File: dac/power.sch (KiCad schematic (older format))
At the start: 47 parts, among them J5 Aux power, Q1 2STD1665T4, U3 OPA1611, U4 MCP1755S-3302E/DB, U5 NCP1117STAT3G, U6 LM337_SOT223

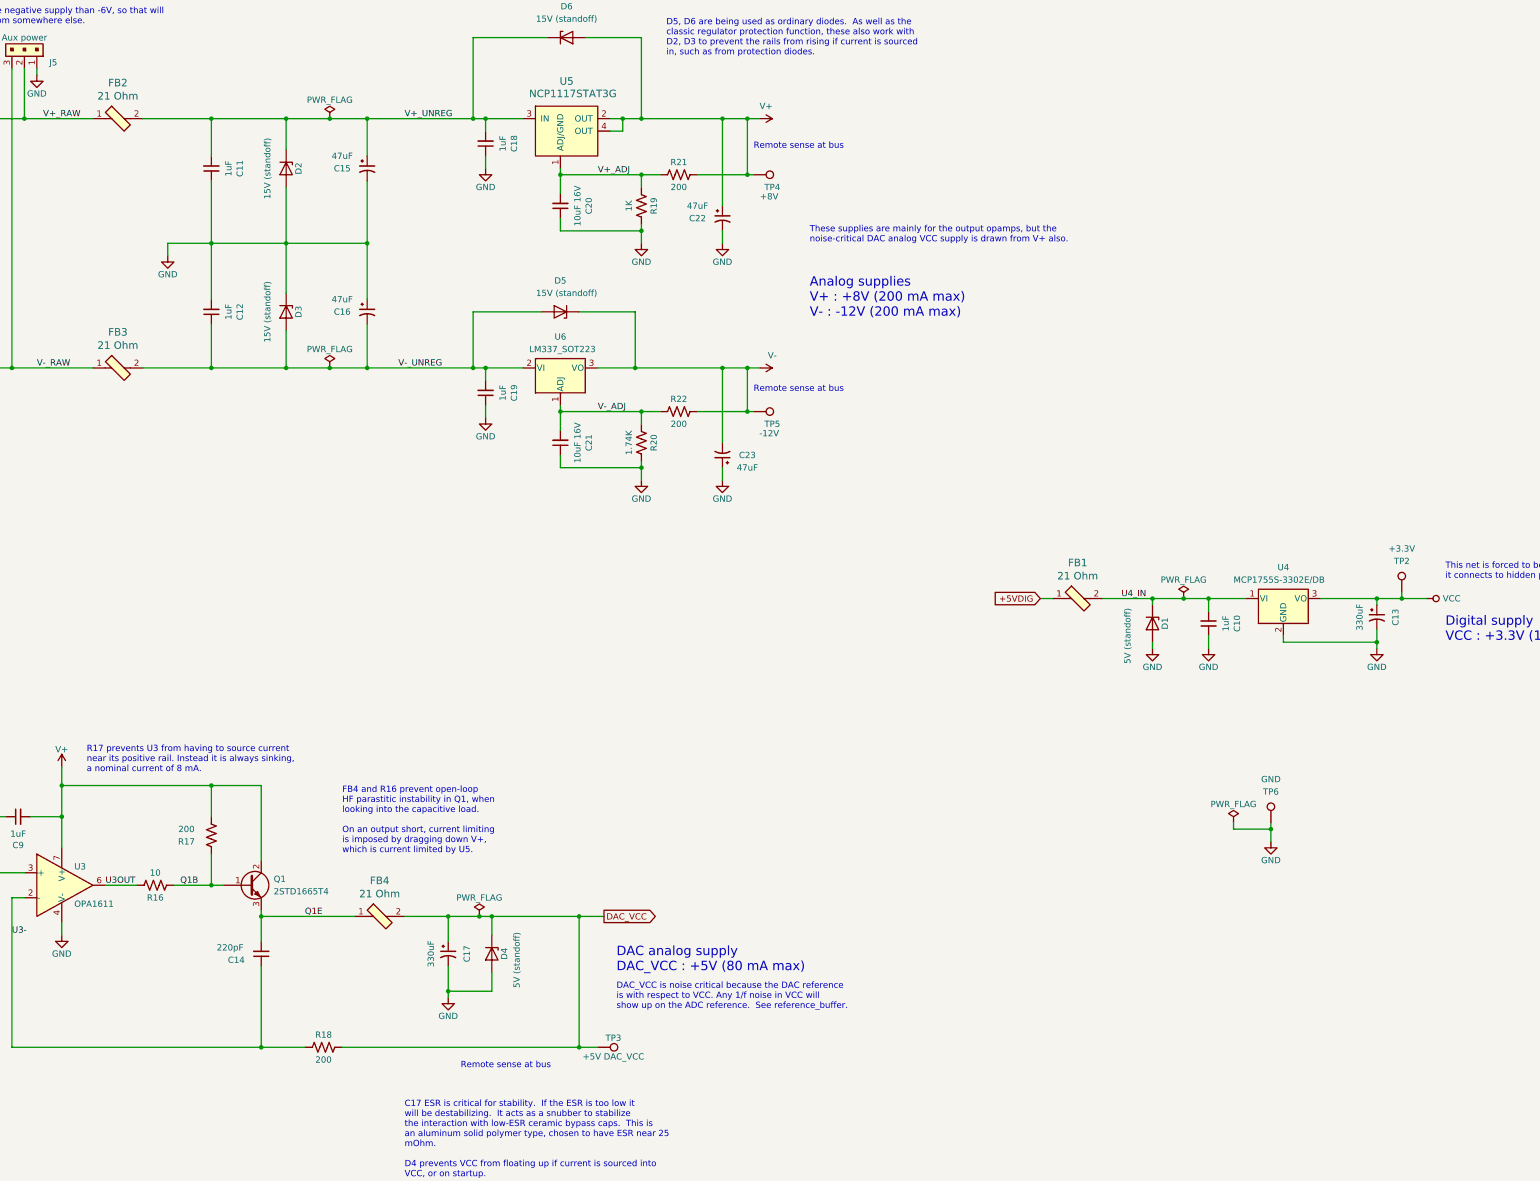
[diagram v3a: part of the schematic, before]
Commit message: Everything seems ready to go for the DAC board.  Made my BOM and checked it twice. Checked footprints of new components and fixed J5, R7-R10.
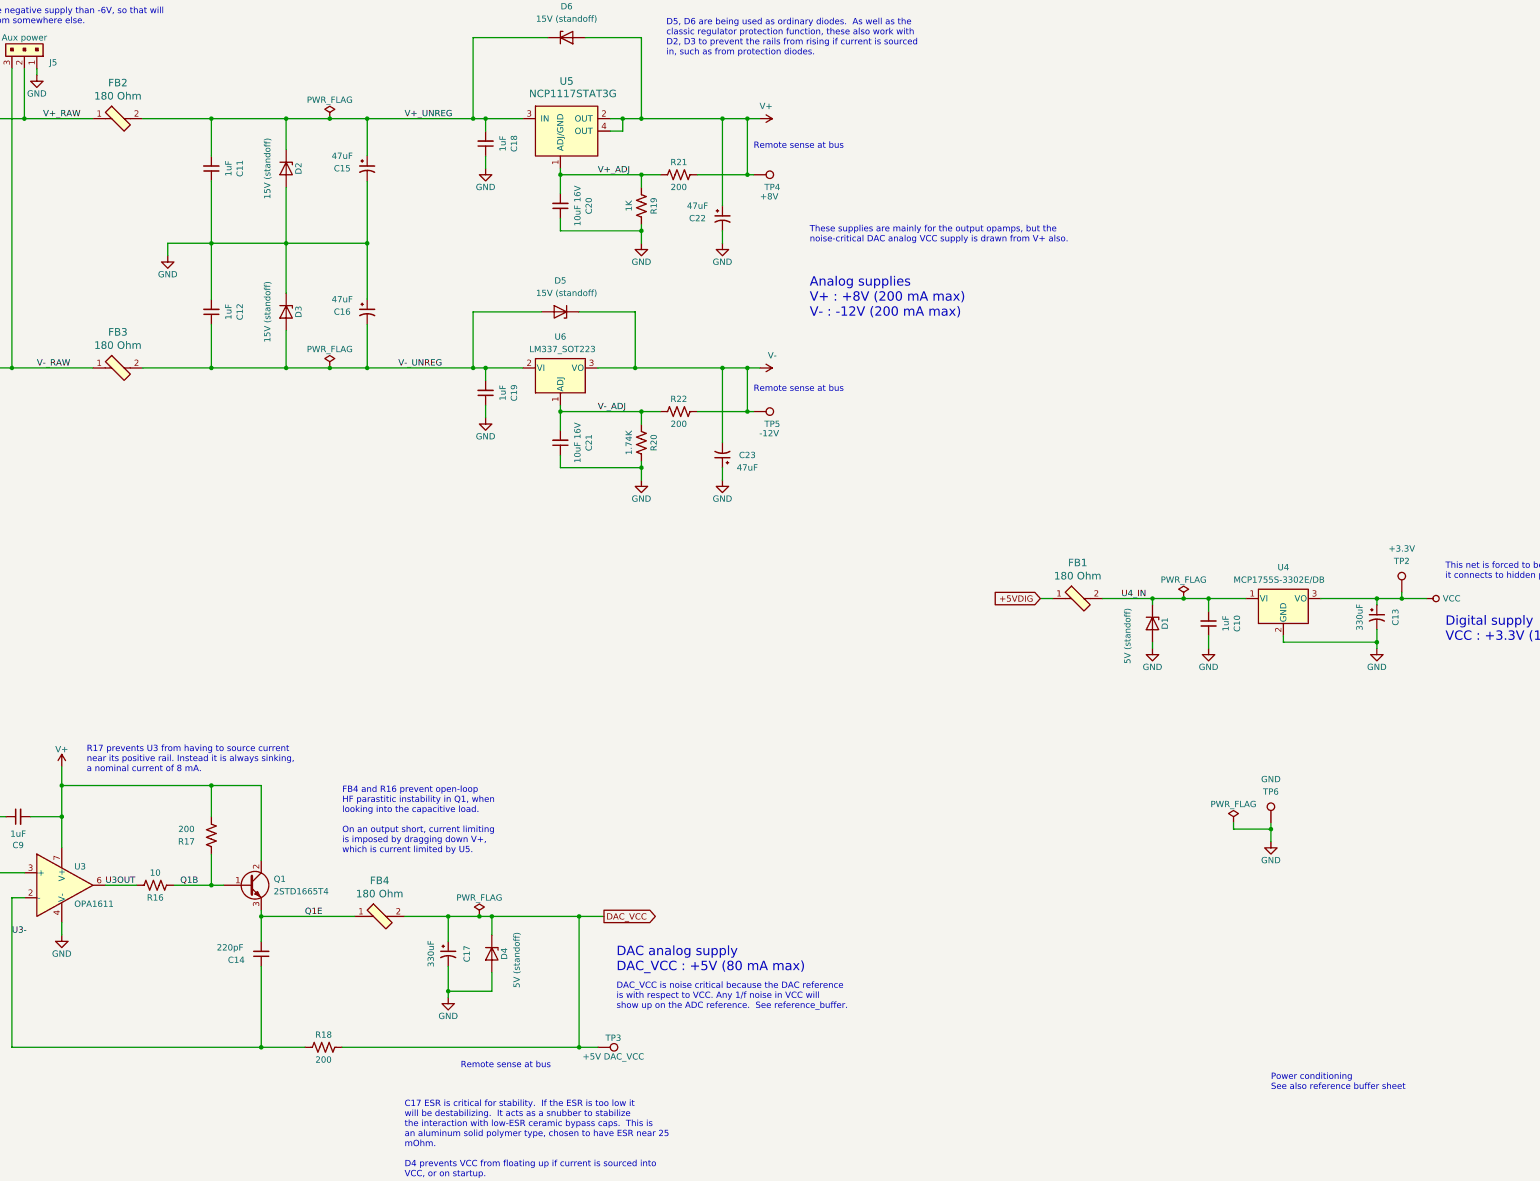
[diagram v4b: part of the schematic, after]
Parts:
- C10, C11, C12, C18, C19, C9: DK line 27 -> I.27
- C13, C17: DK line 19 -> I.19
- C14: DK line 44 -> M.15; Description (none) -> CAP CER 220PF 50V C0G/NP0 0603; Digikey (none) -> 1276-1048-1-ND; MPN (none) -> CL10C221JB8NNNC; Manufacturer (none) -> Samsung Electro-Mechanics
- C15, C16, C22, C23: DK line (none) -> D.5
- C20, C21, C8: DK line 10 -> M.10
- D1, D4: DK line 40 -> I.40
- D2, D3, D5, D6: DK line (none) -> D.39; Description (none) -> TVS DIODE 15V 24.4V SMA; Digikey (none) -> SMAJ15A-FDICT-ND; MPN (none) -> SMAJ15A-13-F; Manufacturer (none) -> Diodes Incorporated
- FB1, FB2, FB3, FB4: value 21 Ohm -> 180 Ohm; DK line 24 -> M.36; Description FERRITE BEAD 21 OHM 0805, 100 nH, 5 mOhm -> FERRITE BEAD 180 OHM 0805 1LN; Digikey 587-1765-1-ND -> 732-6123-1-ND; MPN FBMJ2125HM210NT -> 74279220181; Manufacturer Taiyo Yuden -> Würth Elektronik
- J5: footprint digikey-footprints:PinHeader_1x3_P2.54_Drill1.1mm -> input:molex_kk100_PinHeader_1x3_P2.54_Drill1.1mm; DK line (none) -> D.31; DK_Datasheet_Link https://www.te.com/commerce/DocumentDelivery/DDEController?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 -> (none); DK_Detail_Page /product-detail/en/te-connectivity-amp-connectors/640456-3/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 -> (none); Digi-Key_PN A19470-ND -> (none); Digikey (none) -> WM4201-ND; Family Rectangular Connectors - Headers, Male Pins -> (none); MPN 640456-3 -> 0022232031; Manufacturer TE Connectivity AMP Connectors -> Molex; Status Active -> (none)
- Q1: DK line 22 -> I.22
- R13, R19: DK line (none) -> M.31; Description (none) -> RES 1K OHM 1% 1/8W 0603; Digikey (none) -> RNCP0603FTD1K00CT-ND; MPN (none) -> RNCP0603FTD1K00; Manufacturer (none) -> Stackpole Electronics Inc
- R14, R15: DK line (none) -> M.12; Description (none) -> RES 0 OHM JUMPER 1/10W 0603; Digikey (none) -> RMCF0603ZT0R00CT-ND; MPN (none) -> RMCF0603ZT0R00; Manufacturer (none) -> Stackpole Electronics Inc
- R16: DK line 52 -> I.52
- R17, R18, R21, R22: DK line 55 -> I.55
- R20: DK line (none) -> D.33; Description (none) -> RES 1.74K OHM 1% 1/10W 0603; Digikey (none) -> RMCF0603FT1K74CT-ND; MPN (none) -> RMCF0603FT1K74; Manufacturer (none) -> Stackpole Electronics Inc
- TP2, TP3, TP4, TP5: Description Do Not Populate -> Optional Keystone 5000-5004; Manufacturer (none) -> Keystone Electronics
- TP6: DK line 33 -> I.33
- U3: DK line (none) -> D.2; Description (none) -> IC AUDIO 1 CIRCUIT 8SOIC; Digikey (none) -> 296-47811-1-ND; MPN (none) -> OPA1611AIDR; Manufacturer (none) -> Texas Instruments
- U4: DK line 25 -> I.25
- U5: DK line 26 -> I.26
- U6: DK line (none) -> D.6; Description (none) -> IC REG LIN NEG ADJ 1A SOT223-4; Digikey (none) -> LM337IMPX/NOPBCT-ND; MPN (none) -> LM337IMPX/NOPB; Manufacturer (none) -> Texas Instruments
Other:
- note added: "Power conditioning\nSee also reference buffer sheet"

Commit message: Mainly BOM tweaks, working on setting up more systematic database of parts and BOMs in parts/
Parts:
- R16: DK line I.52 -> I.9; Description RES SMD 10 OHM 5% 1/2W 0805 -> RES SMD 10 OHM 5% 0.4W 0805; MPN CRCW080510R0JNEAHP -> ESR10EZPJ100; Manufacturer Vishay Dale -> Rohm Semiconductor
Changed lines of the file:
@@
 F 1 "10" V 3400 7950 50  0000 C CNN
 F 2 "Resistor_SMD:R_0805_2012Metric" V 3540 7940 50  0001 C CNN
-F 3 "http://www.vishay.com/docs/20043/crcwhpe3.pdf" H 3500 7950 50  0001 C CNN
+F 3 "https://www.rohm.com/datasheet/ESR01MZPF/esr-e" H 3500 7950 50  0001 C CNN
 F 4 "541-10TACT-ND" H 3500 7950 50  0001 C CNN "Digikey"
-F 5 "I.52" H 3500 7950 50  0001 C CNN "DK line"
-F 6 "RES SMD 10 OHM 5% 1/2W 0805" H 3500 7950 50  0001 C CNN "Description"
-F 7 "CRCW080510R0JNEAHP" H 3500 7950 50  0001 C CNN "MPN"
-F 8 "Vishay Dale" H 3500 7950 50  0001 C CNN "Manufacturer"
+F 5 "I.9" H 3500 7950 50  0001 C CNN "DK line"
+F 6 "RES SMD 10 OHM 5% 0.4W 0805" H 3500 7950 50  0001 C CNN "Description"
+F 7 "ESR10EZPJ100" H 3500 7950 50  0001 C CNN "MPN"
+F 8 "Rohm Semiconductor" H 3500 7950 50  0001 C CNN "Manufacturer"
 F 9 "Thick film surge resist" H 3500 7950 50  0001 C CNN "Notes"
 	1    3500 7950

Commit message: BOM change to dac/, start of board revision in input/adc.sch
dac: changed 10 Ohm MPN on BOM

input:
Fixed SOIC-8 footprints
Got rid of bootstrapping of the reference buffer.  Now it runs from the 10 Ohm/330 uF filtered +8/-6.
Changed power input beads from 22 Ohm to 180 Ohm.
Added diode clamp between GND and Earth grounds.
Changed reference buffer to dual opamp.
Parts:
- R16: Digikey 541-10TACT-ND -> RHM10KCT-ND
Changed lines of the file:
@@
 F 2 "Resistor_SMD:R_0805_2012Metric" V 3540 7940 50  0001 C CNN
 F 3 "https://www.rohm.com/datasheet/ESR01MZPF/esr-e" H 3500 7950 50  0001 C CNN
-F 4 "541-10TACT-ND" H 3500 7950 50  0001 C CNN "Digikey"
+F 4 "RHM10KCT-ND" H 3500 7950 50  0001 C CNN "Digikey"
 F 5 "I.9" H 3500 7950 50  0001 C CNN "DK line"
 F 6 "RES SMD 10 OHM 5% 0.4W 0805" H 3500 7950 50  0001 C CNN "Description"

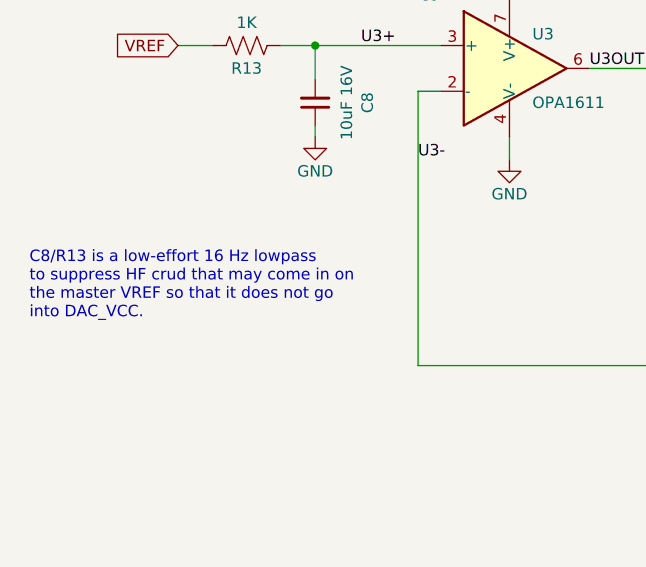
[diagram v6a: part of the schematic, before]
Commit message: Schematic revision for DAC board, compensation tweaks in lv_regs.
Opamp +/- pins were swapped in reference_buffer.sch as side effect of the symbol change from using a dual opamp.

lv_regs files.  The compensation components were (CTUNE/RTUNE) were quite wrong, and everything oscillated like crazy. The positive regulators are fine with no compensation, and the negative regulator benefits from a bit.
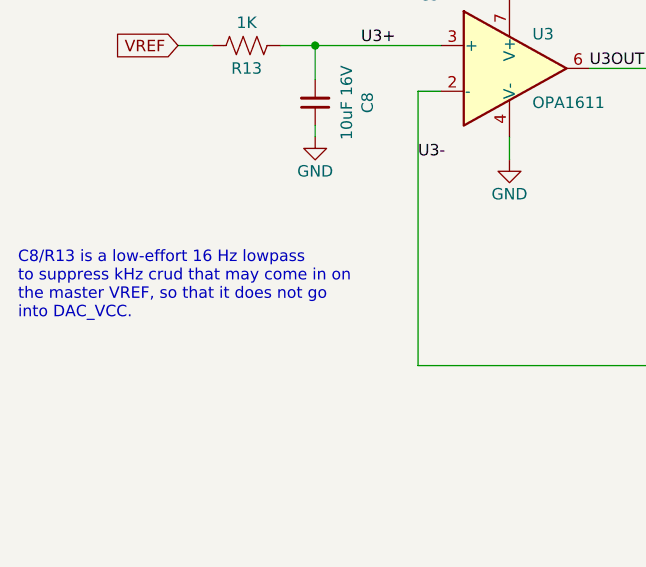
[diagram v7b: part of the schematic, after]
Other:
- note added: "C8/R13 is a low-effort 16 Hz lowpass\nto suppress kHz crud that may come in on\nthe master VREF, so that it does not go\ninto DAC_VCC."
- note removed: "C8/R13 is a low-effort 16 Hz lowpass\nto suppress HF crud that may come in on\nthe master VREF so that it does not go\ninto DAC_VCC."
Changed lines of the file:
@@
 $EndComp
 Connection ~ 6100 8200
-Text Notes 650  9050 0    50   ~ 0
-C8/R13 is a low-effort 16 Hz lowpass\nto suppress HF crud that may come in on\nthe master VREF so that it does not go\ninto DAC_VCC.
+Text Notes 600  9050 0    50   ~ 0
+C8/R13 is a low-effort 16 Hz lowpass\nto suppress kHz crud that may come in on\nthe master VREF, so that it does not go\ninto DAC_VCC.
 $Comp
 L Device:C_Small C?
